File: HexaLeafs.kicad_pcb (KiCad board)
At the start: 2 copper layers, 104 x 90 mm, 21 parts, among them J1 Conn_01x04, J2 Conn_01x04, J3 Conn_01x04, J4 Conn_01x04, J5 Conn_01x04, J6 Conn_01x04, SW1 SW_DIP_x06

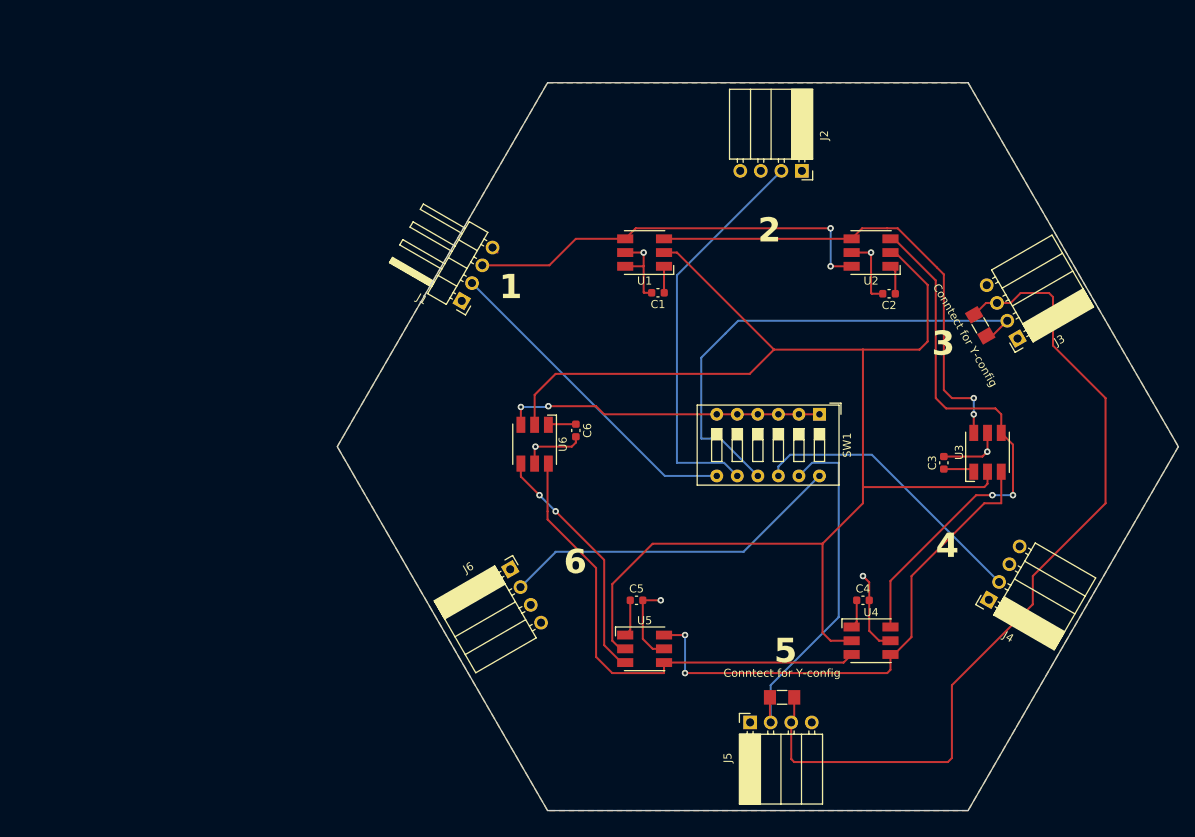
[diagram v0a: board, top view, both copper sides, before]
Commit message: Reworked Layout and added 2nd DIP Switch for optional return path. Added mounting and Tesa Strip cutouts
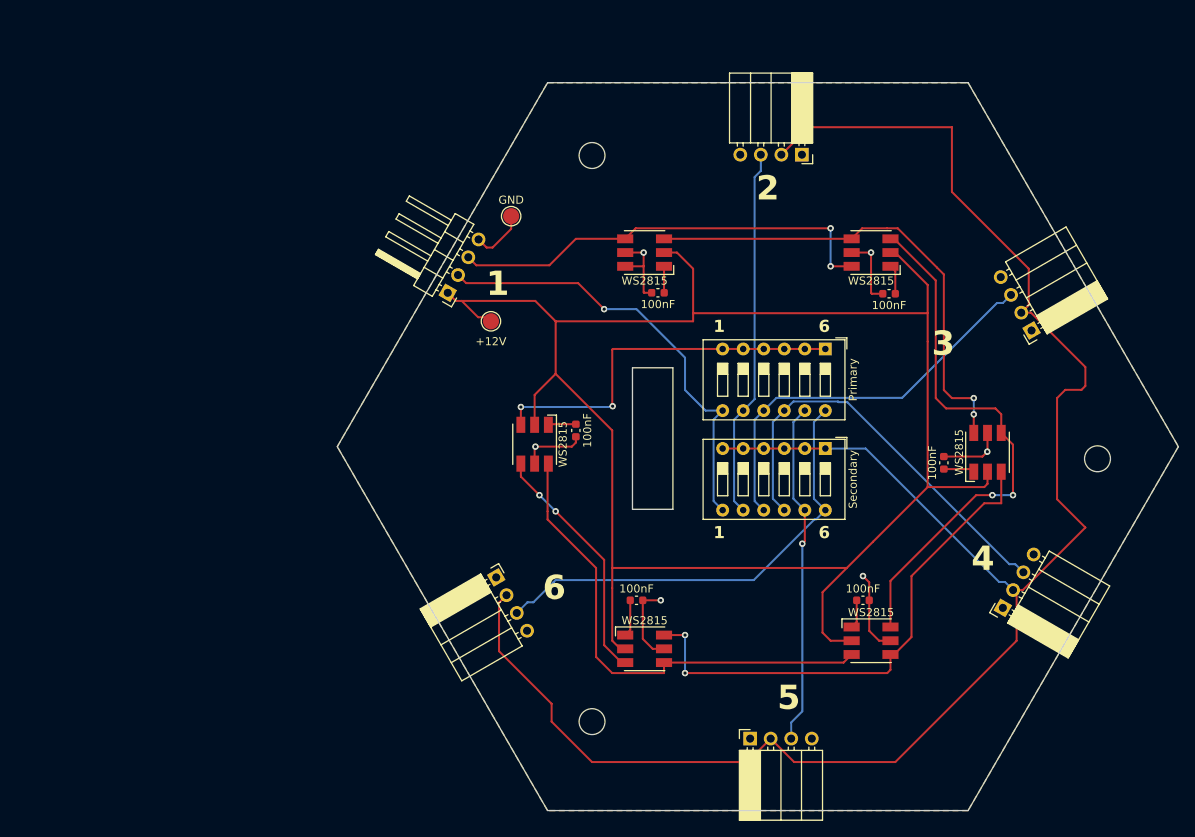
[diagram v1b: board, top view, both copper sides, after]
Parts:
- removed Conntect for Y-config: R_MiniMELF_MMA-0204, Resistor_SMD:R_MiniMELF_MMA-0204 (x2)
- removed SW1: SW_DIP_x06, Button_Switch_THT:SW_DIP_SPSTx06_Slide_9.78x17.42mm_W7.62mm_P2.54mm
- added +12V: TestPoint_Pad_D2.0mm, TestPoint:TestPoint_Pad_D2.0mm, F.Cu at (95.0, 60.5)
- added GND: TestPoint_Pad_D2.0mm, TestPoint:TestPoint_Pad_D2.0mm, F.Cu at (97.5, 47.5)
- added Primary: SW_DIP_x06, Button_Switch_THT:SW_DIP_SPSTx06_Slide_9.78x17.42mm_W7.62mm_P2.54mm, F.Cu at (136.3, 63.9)
- added REF**: MountingHole_3.2mm_M3, MountingHole:MountingHole_3.2mm_M3, F.Cu at (170.0, 77.5)
- added REF**: MountingHole_3.2mm_M3, MountingHole:MountingHole_3.2mm_M3, F.Cu at (107.5, 110.0)
- added REF**: MountingHole_3.2mm_M3, MountingHole:MountingHole_3.2mm_M3, F.Cu at (107.5, 40.0)
- added Secondary: SW_DIP_x06, Button_Switch_THT:SW_DIP_SPSTx06_Slide_9.78x17.42mm_W7.62mm_P2.54mm, F.Cu at (136.3, 76.2)
-  WS2815: renamed from U5
-  WS2815: renamed from U1
-  WS2815: renamed from U6
-  WS2815: renamed from U3
-  WS2815: renamed from U2
-  WS2815: renamed from U4
- moved J1 2.00 mm to (89.7, 57.0)
- moved J3 2.00 mm to (161.8, 61.6)
- moved J6 2.00 mm to (95.7, 92.2)
- moved J4 2.00 mm to (158.3, 95.9)
- moved J2 2.00 mm to (133.4, 39.9)
- moved J5 2.00 mm to (127.0, 112.1)
- renumbered C6 to 100nF, C1 to 100nF, C5 to 100nF, C4 to 100nF, C2 to 100nF, C3 to 100nF
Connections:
- J1 pad 2: Net-(J1-Pin_2) -> Out1
- J2 pad 2: Net-(J2-Pin_2) -> 2nd In
- J2 pad 3: unconnected-(J2-Pin_3-Pad3) -> Out2
- J3 pad 2: Net-(J3-Pin_2) -> 2nd In
- J3 pad 3: (no net) -> Out3
- J4 pad 2: Net-(J4-Pin_2) -> 2nd In
- J4 pad 3: (no net) -> Out4
- J5 pad 2: Net-(J5-Pin_2) -> 2nd In
- J5 pad 3: (no net) -> Out5
- J6 pad 2: Net-(J6-Pin_2) -> 2nd In
- J6 pad 3: (no net) -> Out6
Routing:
- net 2nd In: track 0.00 -> 233.0 mm
- net (no net): track 106.7 -> 0.00 mm
- net Net-(J3-Pin_2): track 62.0 -> 0.00 mm
- net Out6: track 0.00 -> 56.9 mm
- net Out1: track 0.00 -> 55.3 mm, vias 0 -> 1
- net Out4: track 0.00 -> 52.6 mm
- net Out3: track 0.00 -> 49.7 mm
- net Net-(J2-Pin_2): track 49.6 -> 0.00 mm
- net Out2: track 0.00 -> 45.8 mm
- net Net-(J5-Pin_2): track 44.3 -> 0.00 mm
- net +12V: track 182.1 -> 224.9 mm
- net Net-(J6-Pin_2): track 42.7 -> 0.00 mm
- net Out5: track 0.00 -> 42.4 mm, vias 0 -> 1
- net Net-(J1-Pin_2): track 40.1 -> 0.00 mm
- net Net-(J4-Pin_2): track 35.6 -> 0.00 mm
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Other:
- outline, holes or cut-outs redrawn

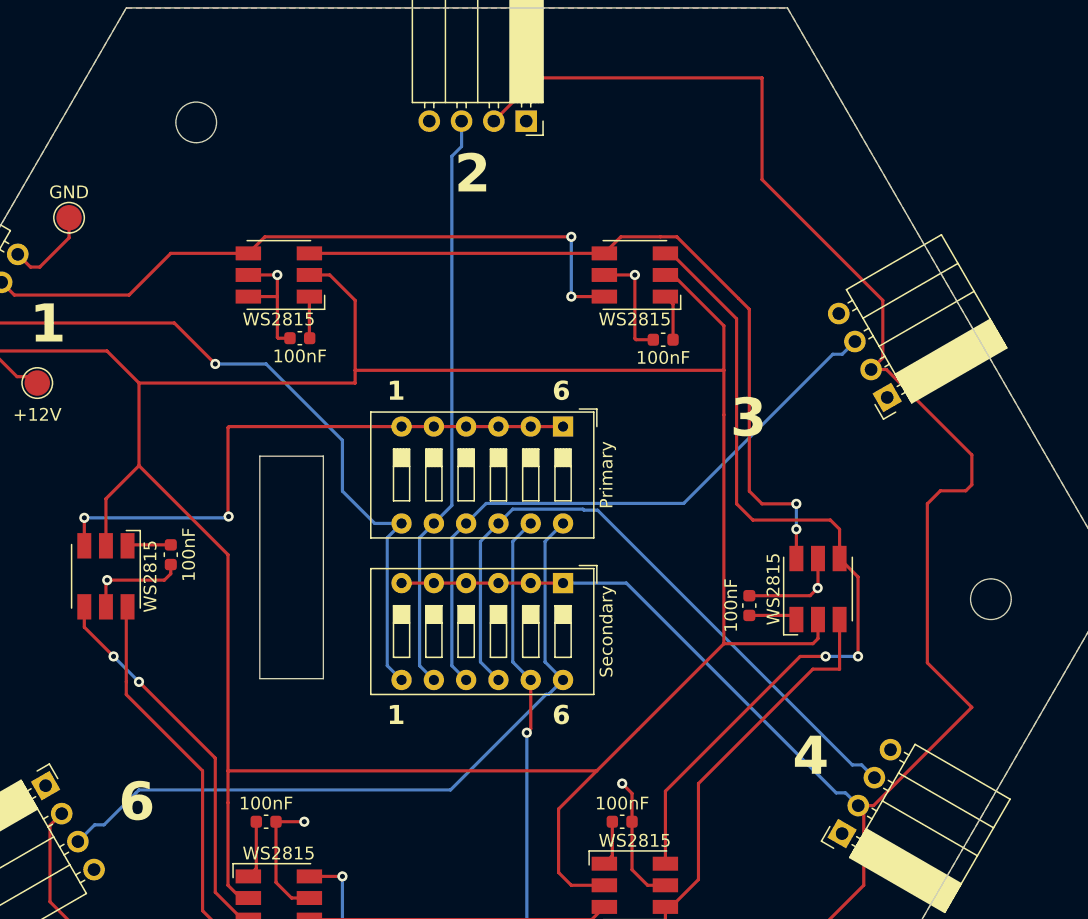
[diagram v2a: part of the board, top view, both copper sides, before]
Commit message: small trace alignments
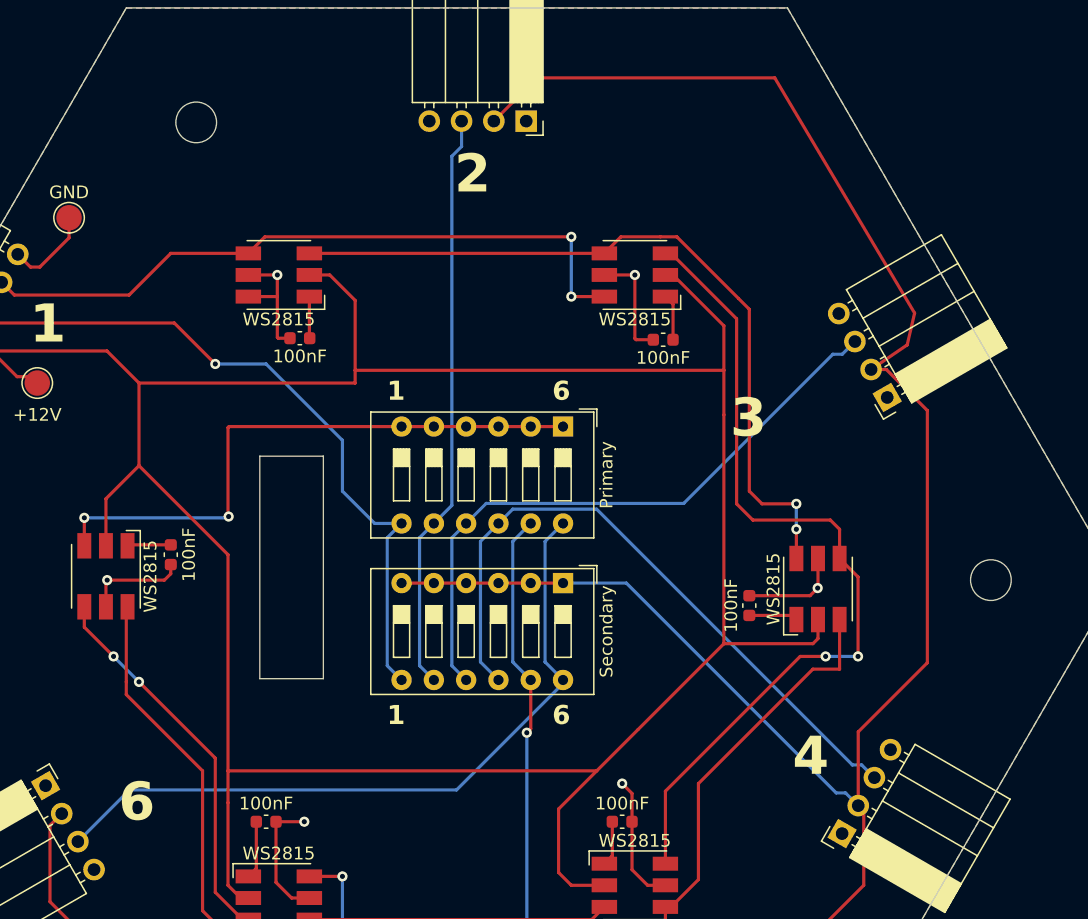
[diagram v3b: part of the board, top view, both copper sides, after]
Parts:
- moved REF** 1.50 mm to (170.0, 76.0)
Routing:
- net 2nd In: track 233.0 -> 226.6 mm
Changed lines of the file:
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@@
 	(footprint "MountingHole:MountingHole_3.2mm_M3"
 		(layer "F.Cu")
-		(at 170 77.5)
+		(at 170 76)
 		(descr "Mounting Hole 3.2mm, no annular, M3")
 		(tags "mounting hole 3.2mm no annular m3")
@@
 	)
 	(segment
-		(start 168.025 68.975)
-		(end 166.025 68.975)
+		(start 160.576539 59.434493)
+		(end 161.77862 59.434493)
 		(width 0.25)
 		(layer "F.Cu")
@@
 	)
 	(segment
-		(start 126.69 115)
-		(end 129.59 112.1)
-		(width 0.25)
-		(layer "F.Cu")
-		(net 18)
-	)
-	(segment
-		(start 168.501556 86.001556)
-		(end 160.76862 93.734493)
+		(start 163.415588 57.5)
+		(end 160.576539 59.434493)
 		(width 0.25)
 		(layer "F.Cu")
@@
 	)
 	(segment
-		(start 152 44.5)
-		(end 161.5 54)
+		(start 126.69 115)
+		(end 129.59 112.1)
 		(width 0.25)
 		(layer "F.Cu")
@@
 	)
 	(segment
-		(start 152 36.5)
-		(end 152 44.5)
-		(width 0.25)
-		(layer "F.Cu")
-		(net 18)
-	)
-	(segment
 		(start 160 100)
 		(end 145 115)
@@
 	)
 	(segment
-		(start 160.576539 59.434493)
-		(end 161.77862 59.434493)
+		(start 164 55)
+		(end 163.415588 57.5)
 		(width 0.25)
 		(layer "F.Cu")
@@
 	)
 	(segment
-		(start 161.5 54)
-		(end 161.5 58.511032)
-		(width 0.25)
-		(layer "F.Cu")
-		(net 18)
-	)
-	(segment
-		(start 161.5 58.511032)
-		(end 160.576539 59.434493)
-		(width 0.25)
-		(layer "F.Cu")
-		(net 18)
-	)
-	(segment
-		(start 165 70)
-		(end 165 82.5)
+		(start 159.566539 87.933461)
+		(end 159.566539 93.734493)
 		(width 0.25)
 		(layer "F.Cu")
@@
 	)
 	(segment
-		(start 96.923461 94.365507)
-		(end 96 95.288968)
+		(start 130.91 39.9)
+		(end 134.31 36.5)
 		(width 0.25)
 		(layer "F.Cu")
@@
 	)
 	(segment
-		(start 168.5 68.5)
-		(end 168.025 68.975)
+		(start 96.923461 94.365507)
+		(end 96 95.288968)
 		(width 0.25)
 		(layer "F.Cu")
@@
 	)
 	(segment
-		(start 161.77862 59.434493)
-		(end 168.5 66.155873)
+		(start 153 36.5)
+		(end 164 55)
 		(width 0.25)
 		(layer "F.Cu")
@@
 	)
 	(segment
-		(start 130.91 39.9)
-		(end 134.31 36.5)
+		(start 96 95.288968)
+		(end 96 101.293072)
 		(width 0.25)
 		(layer "F.Cu")
@@
 	)
 	(segment
-		(start 96 95.288968)
-		(end 96 101.293072)
+		(start 165 82.5)
+		(end 159.566539 87.933461)
 		(width 0.25)
 		(layer "F.Cu")
@@
 	)
 	(segment
-		(start 165 82.5)
-		(end 168.501556 86.001556)
+		(start 161.77862 59.434493)
+		(end 165 62.655873)
 		(width 0.25)
 		(layer "F.Cu")
@@
 	)
 	(segment
-		(start 166.025 68.975)
-		(end 165 70)
-		(width 0.25)
-		(layer "F.Cu")
-		(net 18)
-	)
-	(segment
-		(start 160.76862 93.734493)
-		(end 159.566539 93.734493)
-		(width 0.25)
-		(layer "F.Cu")
-		(net 18)
-	)
-	(segment
-		(start 168.5 66.155873)
-		(end 168.5 68.5)
+		(start 134.31 36.5)
+		(end 153 36.5)
 		(width 0.25)
 		(layer "F.Cu")
@@
 	)
 	(segment
-		(start 134.31 36.5)
-		(end 152 36.5)
+		(start 165 62.655873)
+		(end 165 82.5)
 		(width 0.25)
 		(layer "F.Cu")
@@
 	)
 	(segment
-		(start 137.9175 70.4175)
-		(end 138 70.5)
+		(start 138.987199 70.4175)
+		(end 159.104488 90.534789)
 		(width 0.25)
 		(layer "B.Cu")
@@
 	)
 	(segment
-		(start 159.836539 90.534789)
-		(end 160.836539 91.534789)
-		(width 0.25)
-		(layer "B.Cu")
-		(net 20)
-	)
-	(segment
-		(start 131.27 71.5425)
-		(end 132.395 70.4175)
-		(width 0.25)
-		(layer "B.Cu")
-		(net 20)
-	)
-	(segment
 		(start 129.855 72.9575)
 		(end 131.27 71.5425)
@@
 	)
 	(segment
-		(start 138 70.5)
-		(end 139.069699 70.5)
+		(start 132.395 70.4175)
+		(end 138.987199 70.4175)
 		(width 0.25)
 		(layer "B.Cu")
@@
 	)
 	(segment
-		(start 131.27 83.8525)
-		(end 129.855 82.4375)
+		(start 131.27 71.5425)
+		(end 132.395 70.4175)
 		(width 0.25)
 		(layer "B.Cu")
@@
 	)
 	(segment
-		(start 139.069699 70.5)
-		(end 159.104488 90.534789)
+		(start 131.27 83.8525)
+		(end 129.855 82.4375)
 		(width 0.25)
 		(layer "B.Cu")
@@
 	)
 	(segment
-		(start 132.395 70.4175)
-		(end 137.9175 70.4175)
+		(start 159.836539 90.534789)
+		(end 160.836539 91.534789)
 		(width 0.25)
 		(layer "B.Cu")
@@
 	)
 	(segment
-		(start 133.81 83.8525)
+		(start 133.5 88)
 		(end 133.81 87.69)
 		(width 0.25)
@@
 	(segment
 		(start 133.81 87.69)
-		(end 133.5 88)
+		(end 133.81 83.8525)
 		(width 0.25)
 		(layer "F.Cu")
@@
 	)
 	(segment
-		(start 132.13 110.1)
-		(end 132.13 112.1)
+		(start 133.5 108.73)
+		(end 132.13 110.1)
 		(width 0.25)
 		(layer "B.Cu")
@@
 	)
 	(segment
-		(start 133.81 83.8525)
-		(end 132.395 82.4375)
+		(start 133.5 88)
+		(end 133.5 108.73)
 		(width 0.25)
 		(layer "B.Cu")
@@
 	)
 	(segment
-		(start 132.395 72.9575)
-		(end 133.81 71.5425)
+		(start 133.81 83.8525)
+		(end 132.395 82.4375)
 		(width 0.25)
 		(layer "B.Cu")
@@
 	)
 	(segment
-		(start 133.5 108.73)
-		(end 132.13 110.1)
+		(start 132.13 110.1)
+		(end 132.13 112.1)
 		(width 0.25)
 		(layer "B.Cu")
@@
 	)
 	(segment
-		(start 132.395 82.4375)
-		(end 132.395 72.9575)
+		(start 132.395 72.9575)
+		(end 133.81 71.5425)
 		(width 0.25)
 		(layer "B.Cu")
@@
 	)
 	(segment
-		(start 133.5 88)
-		(end 133.5 108.73)
+		(start 132.395 82.4375)
+		(end 132.395 72.9575)
 		(width 0.25)
 		(layer "B.Cu")
@@
 	)
 	(segment
-		(start 100.245362 95.245362)
-		(end 99.51331 95.245362)
+		(start 102.258672 92.5)
+		(end 127.974695 92.5)
 		(width 0.25)
 		(layer "B.Cu")
@@
 	)
 	(segment
-		(start 100.245362 95.245362)
-		(end 102.745362 92.745362)
+		(start 127.974695 92.5)
+		(end 136.35 84.124695)
 		(width 0.25)
 		(layer "B.Cu")
@@
 	)
 	(segment
-		(start 99.51331 95.245362)
-		(end 98.193461 96.565211)
+		(start 136.35 84.124695)
+		(end 136.35 83.8525)
 		(width 0.25)
 		(layer "B.Cu")
@@
 	)
 	(segment
-		(start 136.35 83.8525)
-		(end 135.225 84.9775)
-		(width 0.25)
-		(layer "B.Cu")
-		(net 22)
-	)
-	(segment
-		(start 102.990724 92.5)
-		(end 102.745362 92.745362)
-		(width 0.25)
-		(layer "B.Cu")
-		(net 22)
-	)
-	(segment
-		(start 135.225 84.9775)
-		(end 135.0225 84.9775)
+		(start 98.193461 96.565211)
+		(end 102.258672 92.5)
 		(width 0.25)
 		(layer "B.Cu")
@@
 	)
 	(segment
-		(start 135.0225 84.9775)
-		(end 127.5 92.5)
-		(width 0.25)
-		(layer "B.Cu")
-		(net 22)
-	)
-	(segment
 		(start 136.35 83.8525)
 		(end 134.935 82.4375)
 		(width 0.25)
 		(layer "B.Cu")
-		(net 22)
-	)
-	(segment
-		(start 127.5 92.5)
-		(end 102.990724 92.5)
-		(width 0.25)
-		(layer "B.Cu")

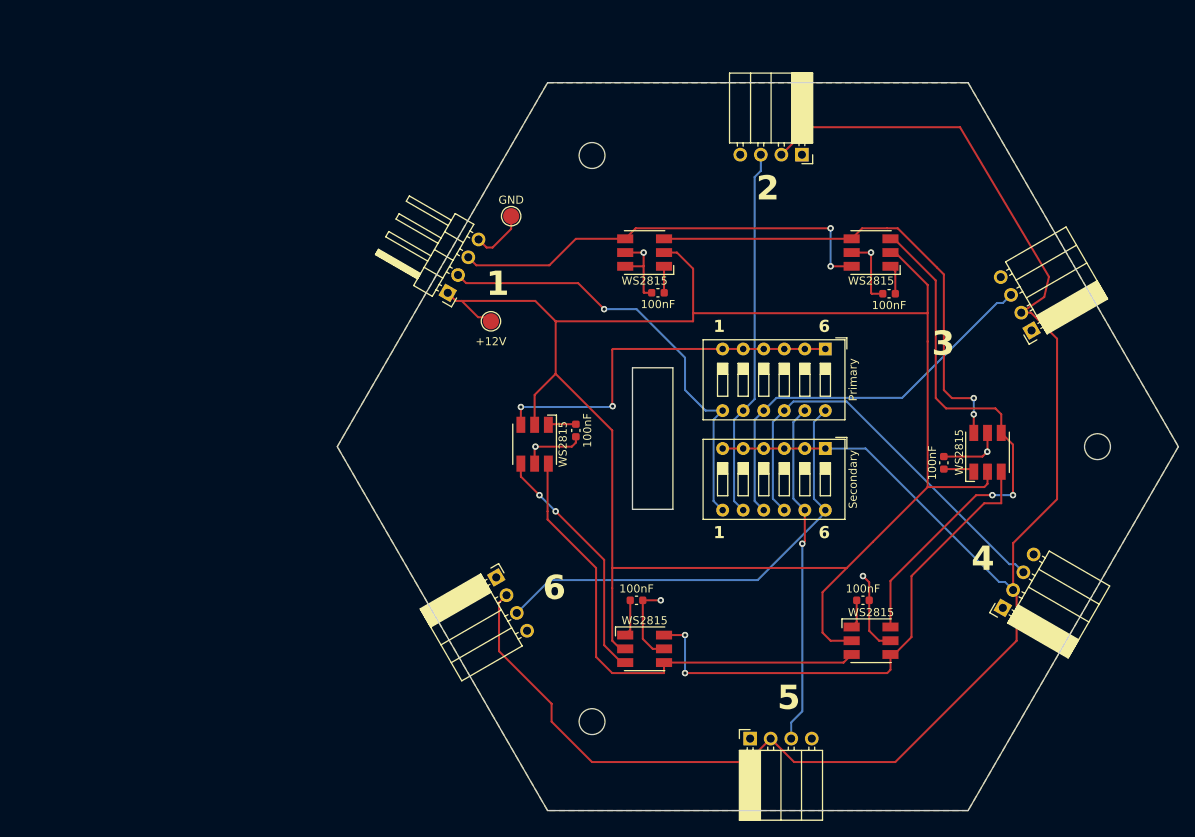
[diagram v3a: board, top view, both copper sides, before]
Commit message: align female connectores
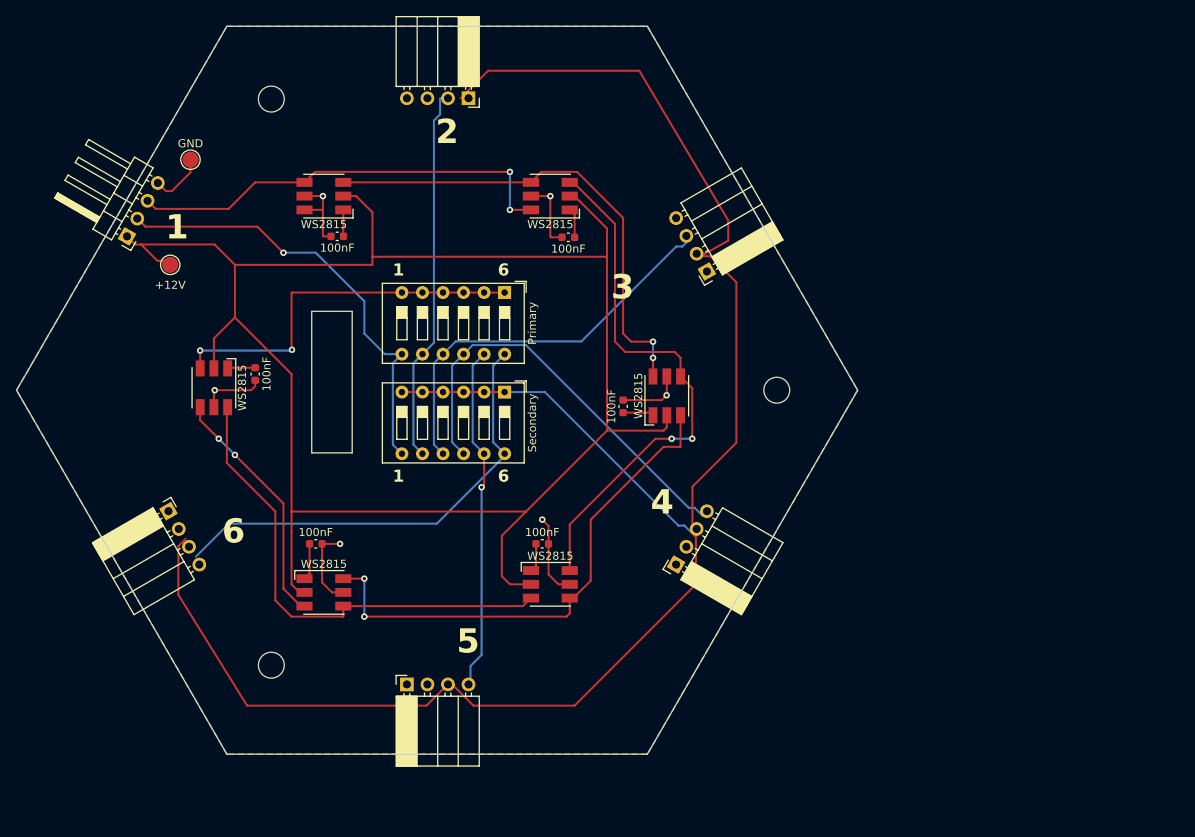
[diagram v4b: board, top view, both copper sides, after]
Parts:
- removed J3, J4, J5, J6: Conn_01x04, Connector_PinSocket_2.54mm:PinSocket_1x04_P2.54mm_Horizontal
- added J2: Conn_01x04, Connector_PinSocket_2.54mm:PinSocket_1x04_P2.54mm_Horizontal, F.Cu at (57.0, 87.3)
- added J2: Conn_01x04, Connector_PinSocket_2.54mm:PinSocket_1x04_P2.54mm_Horizontal, F.Cu at (119.8, 51.0)
- added J2: Conn_01x04, Connector_PinSocket_2.54mm:PinSocket_1x04_P2.54mm_Horizontal, F.Cu at (88.4, 105.4)
- added J2: Conn_01x04, Connector_PinSocket_2.54mm:PinSocket_1x04_P2.54mm_Horizontal, F.Cu at (119.8, 87.3)
- moved J2 45.6 mm to (88.4, 32.9)
- moved  WS2815 40.3 mm to (60.7, 68.7)
- moved  WS2815 40.3 mm to (116.7, 69.7)
- moved REF** 40.3 mm to (130.3, 69.0)
- moved +12V 40.3 mm to (55.3, 53.5)
- moved GND 40.3 mm to (57.8, 40.5)
- moved  WS2815 40.3 mm to (74.3, 94.0)
- moved  WS2815 40.3 mm to (74.3, 45.0)
- moved  WS2815 40.3 mm to (102.3, 45.0)
- moved  WS2815 40.3 mm to (102.3, 93.0)
- moved 100nF 40.3 mm to (65.8, 67.0)
- moved 100nF 40.3 mm to (76.0, 50.0)
- moved 100nF 40.3 mm to (73.3, 88.0)
- moved 100nF 40.3 mm to (101.3, 88.0)
- moved 100nF 40.3 mm to (104.6, 50.1)
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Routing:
- net +12V: track 224.9 -> 409.4 mm
- net 2nd In: track 226.6 -> 43.2 mm
